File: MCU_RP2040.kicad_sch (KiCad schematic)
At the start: 30 parts, among them Q1 2N7002PV,115, SW100 EVPAA202K, U4 W25Q128JVSIQ, U5 RP2040, X1 ECS-2520MVLC-120-CN

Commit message: Review Schematic, Add TRS connector. Continue routing
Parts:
- removed C8: 10uF, Capacitor_SMD:C_0805_2012Metric, symbol Device:C_Small
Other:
- moved on the sheet: C21, C9, Q1B, R11, R12

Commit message: Continue routing.
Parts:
- X1: footprint Mad_Footprints:Oscillator_SMD_ECS_2520MV-xxx-xx-4Pin_2.5x2.0mm -> Oscillator:Oscillator_SMD_ECS_2520MV-xxx-xx-4Pin_2.5x2.0mm; symbol Mad_Symbols:ECS-2520MV-xxx-xx -> Mad_Symbols:ECS-2520MV
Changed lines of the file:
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@@
 			)
 		)
-		(property "Datasheet" "https://www.yageo.com/upload/media/product/products/datasheet/rchip/PYu-RC_Group_51_RoHS_L_12.pdf"
+		(property "Datasheet" "~"
 			(at 58.42 162.56 0)
 			(effects
@@
 			)
 		)
-		(property "Description" "10 kOhms ±1% 0.063W, 1/16W Chip Resistor 0402 (1005 Metric) Moisture Resistant Thick Film"
+		(property "Description" "Resistor, small symbol"
 			(at 58.42 162.56 0)
 			(effects
@@
 			)
 		)
-		(property "Datasheet" "https://www.yageo.com/upload/media/product/products/datasheet/rchip/PYu-RC_Group_51_RoHS_L_12.pdf"
+		(property "Datasheet" "~"
 			(at 48.26 187.96 0)
 			(effects
@@
 			)
 		)
-		(property "Description" "10 kOhms ±1% 0.063W, 1/16W Chip Resistor 0402 (1005 Metric) Moisture Resistant Thick Film"
+		(property "Description" "Resistor, small symbol"
 			(at 48.26 187.96 0)
 			(effects
@@
 	)
 	(symbol
-		(lib_id "Mad_Symbols:ECS-2520MV-xxx-xx")
+		(lib_id "Mad_Symbols:ECS-2520MV")
 		(at 72.39 74.93 0)
 		(unit 1)
@@
 			)
 		)
-		(property "Footprint" "Mad_Footprints:Oscillator_SMD_ECS_2520MV-xxx-xx-4Pin_2.5x2.0mm"
-			(at 74.803 85.217 0)
+		(property "Footprint" "Oscillator:Oscillator_SMD_ECS_2520MV-xxx-xx-4Pin_2.5x2.0mm"
+			(at 72.136 83.566 0)
 			(effects
 				(font
@@
 		)
 		(property "Datasheet" "https://www.ecsxtal.com/store/pdf/ECS-2520MV.pdf"
-			(at 58.928 73.152 0)
+			(at 72.898 85.344 0)
 			(effects
 				(font
@@
 			)
 		)
-		(property "Description" "12 MHz XO (Standard) CMOS Oscillator 1.6V ~ 3.6V Enable/Disable 4-SMD, No Lead"
-			(at 63.373 76.327 0)
+		(property "Description" "HCMOS Crystal Clock Oscillator, 2.5x2.0 mm SMD"
+			(at 77.343 88.519 0)
 			(effects
 				(font
@@
 			)
 		)
+		(property "Config" ""
+			(at 72.39 74.93 0)
+			(effects
+				(font
+					(size 1.27 1.27)
+				)
+				(hide yes)
+			)
+		)
 		(pin "3"
 		)
@@
 		)
 		(property "Footprint" "Diode_SMD:D_SOD-523"
-			(at 53.34 172.72 0)
+			(at 53.34 178.562 0)
 			(effects
 				(font
@@
 		)
 		(property "Datasheet" "https://www.onsemi.com/pdf/datasheet/rb520s30t1-d.pdf"
-			(at 53.34 172.72 0)
+			(at 53.848 175.006 0)
 			(effects
 				(font
 					(size 1.27 1.27)
+					(thickness 0.1588)
 				)
 				(hide yes)
@@
 		)
 		(property "Description" "Diode 30 V 200mA Surface Mount SOD-523"
-			(at 53.34 172.72 0)
+			(at 53.34 176.784 0)
 			(effects
 				(font
@@
 		)
 		(property "Rating" "DIODE SCHOTTKY 30V 200MA SOD523"
-			(at 53.34 172.72 0)
+			(at 53.34 176.784 0)
 			(effects
 				(font
@@
 		)
 		(property "Supplier" "Digikey"
-			(at 53.34 172.72 0)
+			(at 53.594 181.61 0)
 			(effects
 				(font
@@
 		)
 		(property "Supplier PN" "RB520S30T5GOSCT-ND"
-			(at 53.34 172.72 0)
+			(at 53.34 180.086 0)
 			(effects
 				(font
@@
 			)
 		)
+		(property "Config" ""
+			(at 53.34 172.72 0)
+			(effects
+				(font
+					(size 1.27 1.27)
+				)
+				(hide yes)
+			)
+		)
 		(pin "1"
 		)
@@
 			)
 		)
-		(property "Datasheet" "https://www.yageo.com/upload/media/product/products/datasheet/rchip/PYu-RC_Group_51_RoHS_L_12.pdf"
+		(property "Datasheet" "~"
 			(at 78.74 187.96 0)
 			(effects
@@
 			)
 		)
-		(property "Description" "51 kOhms ±1% 0.063W, 1/16W Chip Resistor 0402 (1005 Metric) Moisture Resistant Thick Film"
+		(property "Description" "Resistor, small symbol"
 			(at 78.74 187.96 0)
 			(effects
@@
 			)
 		)
-		(property "Datasheet" "https://www.yageo.com/upload/media/product/products/datasheet/rchip/PYu-RC_Group_51_RoHS_L_12.pdf"
+		(property "Datasheet" "~"
 			(at 100.33 162.56 0)
 			(effects
@@
 			)
 		)
-		(property "Description" "1 kOhms ±1% 0.063W, 1/16W Chip Resistor 0402 (1005 Metric) Moisture Resistant Thick Film"
+		(property "Description" "Resistor, small symbol"
 			(at 100.33 162.56 0)
 			(effects
@@
 			)
 		)
-		(property "Datasheet" "https://www.yageo.com/upload/media/product/products/datasheet/rchip/PYu-RC_Group_51_RoHS_L_12.pdf"
+		(property "Datasheet" "~"
 			(at 64.77 172.72 0)
 			(effects
@@
 			)
 		)
-		(property "Description" "51 kOhms ±1% 0.063W, 1/16W Chip Resistor 0402 (1005 Metric) Moisture Resistant Thick Film"
+		(property "Description" "Resistor, small symbol"
 			(at 64.77 172.72 0)
 			(effects
@@
 			)
 		)
-		(property "Datasheet" "https://www.yageo.com/upload/media/product/products/datasheet/rchip/PYu-RC_Group_51_RoHS_L_12.pdf"
+		(property "Datasheet" "~"
 			(at 78.74 179.07 0)
 			(effects
@@
 			)
 		)
-		(property "Description" "51 kOhms ±1% 0.063W, 1/16W Chip Resistor 0402 (1005 Metric) Moisture Resistant Thick Film"
+		(property "Description" "Resistor, small symbol"
 			(at 78.74 179.07 0)
 			(effects
@@
 			)
 		)
-		(property "Datasheet" "https://www.yageo.com/upload/media/product/products/datasheet/rchip/PYu-RC_Group_51_RoHS_L_12.pdf"
+		(property "Datasheet" "~"
 			(at 83.82 158.75 0)
 			(effects
@@
 			)
 		)
-		(property "Description" "10 kOhms ±1% 0.063W, 1/16W Chip Resistor 0402 (1005 Metric) Moisture Resistant Thick Film"
+		(property "Description" "Resistor, small symbol"
 			(at 83.82 158.75 0)
 			(effects
@@
 			)
 		)
-		(property "Datasheet" "https://www.yageo.com/upload/media/product/products/datasheet/rchip/PYu-RC_Group_51_RoHS_L_12.pdf"
+		(property "Datasheet" "~"
 			(at 90.17 72.39 0)
 			(effects
@@
 			)
 		)
-		(property "Description" "1 kOhms ±1% 0.063W, 1/16W Chip Resistor 0402 (1005 Metric) Moisture Resistant Thick Film"
+		(property "Description" "Resistor, small symbol"
 			(at 90.17 72.39 0)
 			(effects

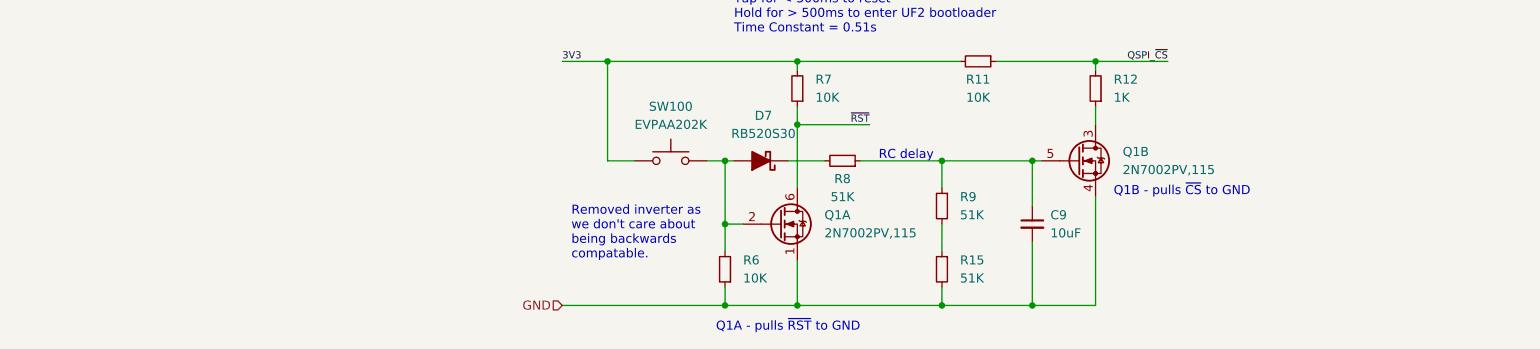
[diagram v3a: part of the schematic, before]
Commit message: Update to 0603 components
Update part of PCB

Finish re-routing 0603

adjust workflow for refactored kibot-config

fill zones to fix FIDs
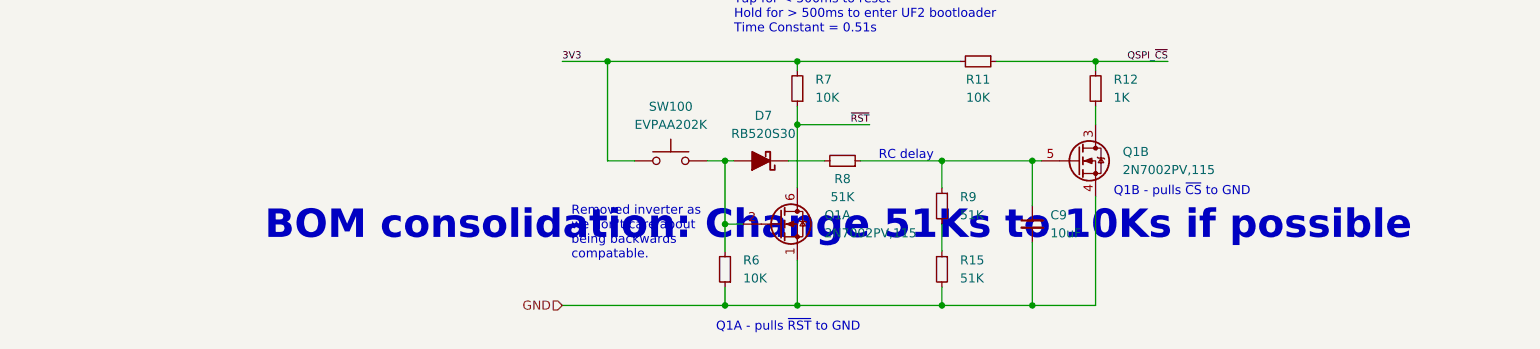
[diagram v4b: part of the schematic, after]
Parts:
- C10, C11, C12, C14, C16, C17, C18, C19, C20, C21, C6, C7: footprint Capacitor_SMD:C_0402_1005Metric -> Capacitor_SMD:C_0603_1608Metric; MPN CC0402KPX7R9BB104 -> CC0603KPX7R9BB104; Price $0.17 -> $0.10; Rating CAP 0402 50V 100 NF X7R -> CAP CER 0.1UF 50V X7R 0603; Supplier PN 13-CC0402KPX7R9BB104CT-ND -> 311-3567-1-ND
- R10, R12: footprint Resistor_SMD:R_0402_1005Metric -> Resistor_SMD:R_0603_1608Metric; MPN RC0402FR-071KL -> RC0603FR-071KL; Price $0.16 -> $0.10; Rating RES 1K OHM 1% 1/16W 0402 -> RES 1K OHM 1% 1/16W 0603; Supplier PN 311-1.00KLRCT-ND -> 311-1.00KHRCT-ND
- R11, R6, R7: footprint Resistor_SMD:R_0402_1005Metric -> Resistor_SMD:R_0603_1608Metric; MPN RC0402FR-0710KL -> RC0603FR-0710KL; Price $0.16 -> $0.10; Rating RES 10K OHM 1% 1/16W 0402 -> RES 10K OHM 1% 1/16W 0603; Supplier PN 311-10.0KLRCT-ND -> 311-10.0KHRCT-ND
- R15, R8, R9: footprint Resistor_SMD:R_0402_1005Metric -> Resistor_SMD:R_0603_1608Metric; MPN RC0402FR-0751KL -> RC0603FR-0751KL; Price $0.16 -> $0.10; Rating RES 51K OHM 1% 1/16W 0402 -> RES 51K OHM 1% 1/16W 0603; Supplier PN 311-51.0KLRCT-ND -> 311-51.0KHRCT-ND
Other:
- note added: "BOM consolidation: Change 51Ks to 10Ks if possible"

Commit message: Remove BOM consolidation comment
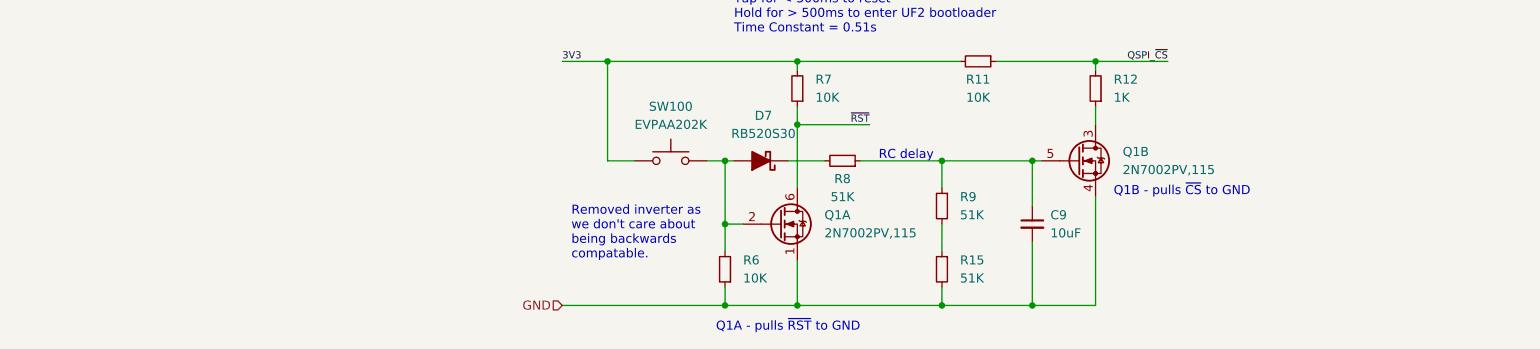
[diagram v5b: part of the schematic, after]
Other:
- note removed: "BOM consolidation: Change 51Ks to 10Ks if possible"
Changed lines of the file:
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@@
-		)
-	)
-	(text "BOM consolidation: Change 51Ks to 10Ks if possible"
-		(exclude_from_sim no)
-		(at 144.78 184.15 0)
-		(effects
-			(font
-				(size 4 4)
-				(thickness 0.8)
-				(bold yes)
-			)
-			(justify right bottom)
 		)
 	)

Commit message: Updates component supplier information
Replaces supplier part numbers with LCSC, Digikey and Mouser numbers
for better component sourcing and availability tracking.

Removes redundant "Supplier PN", "Substitute", and "LCSC PN" properties.
Hides some BOM columns in the project settings.

Also fixes a couple of pin UUIDs and config flags.
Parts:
- C10, C11, C12, C14, C16, C17, C18, C19, C20, C21, C6, C7: Supplier PN 311-3567-1-ND -> (none); digikey (none) -> 311-3567-1-ND; mouser (none) -> 603-CC603KPX7R9BB104
- C13, C15: Supplier PN 311-1445-1-ND -> (none); digikey (none) -> 311-1445-1-ND; mouser (none) -> 603-CC603KRX5R8BB105
- C9: Supplier PN 311-1869-1-ND -> (none); digikey (none) -> 311-1869-1-ND; mouser (none) -> 603-CC805KKX5R8BB106
- D7: Supplier PN RB520S30T5GOSCT-ND -> (none); digikey (none) -> RB520S30T5GOSCT-ND; mouser (none) -> 863-RB520S30T5G
- Q1: Supplier PN 1727-4792-1-ND -> (none); digikey (none) -> 1727-4792-1-ND; mouser (none) -> 771-2N7002PV-115
- R10, R12: Supplier PN 311-1.00KHRCT-ND -> (none); digikey (none) -> 311-1.00KHRCT-ND; mouser (none) -> 603-RC0603FR-071KL
- R11, R6, R7: Supplier PN 311-10.0KHRCT-ND -> (none); digikey (none) -> 311-10.0KHRCT-ND; mouser (none) -> 603-RC0603FR-0710KL
- R15, R8, R9: Supplier PN 311-51.0KHRCT-ND -> (none); digikey (none) -> 311-51.0KHRCT-ND; mouser (none) -> 603-RC0603FR-0751KL
- SW100: Supplier PN P13348SCT-ND -> (none); digikey (none) -> P13348SCT-ND; mouser (none) -> 667-EVP-AA202K
- U4: Supplier PN W25Q128JVSIQ-ND -> (none); digikey (none) -> W25Q128JVSIQ-ND
- U5: Supplier PN 2648-SC0914(13)CT-ND -> (none); digikey (none) -> 2648-SC0914(13)CT-ND; mouser (none) -> 358-SC091413
- X1: Supplier PN 50-ECS-2520MVLC-120-CN-TRCT-ND -> (none); digikey (none) -> 50-ECS-2520MVLC-120-CN-TRCT-ND; mouser (none) -> 520-2520MVLC-120CNTR
